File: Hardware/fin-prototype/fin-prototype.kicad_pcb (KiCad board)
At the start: 4 copper layers, 50 x 50 mm, 80 parts, among them J1 USB_C_Receptacle_USB2.0_16P, J10 Conn_01x01_Pin, J11 Conn_01x01_Pin, J12 Conn_01x01_Pin, J13 Conn_01x01_Pin, J14 Conn_01x01_Pin, J15 Conn_01x01_Pin, J16 Conn_01x01_Pin, J17 Conn_01x01_Pin, J18 Conn_01x01_Pin, J2 Conn_01x04_Pin, J3 Conn_01x04_Pin, J4 Conn_01x08_Pin, J5 Conn_01x04_Pin, J6 Conn_01x01_Pin, J7 Conn_01x01_Pin, J8 Conn_01x01_Pin, J9 Conn_01x01_Pin, SW1 SW_Push, SW2 SW_Push, U1 ADS131M03QPWRQ1, U2 STM32L412C8Tx, U3 W25N512GVEIG, U4 TMP235A4DBZR, U5 FT232RNQ-REEL

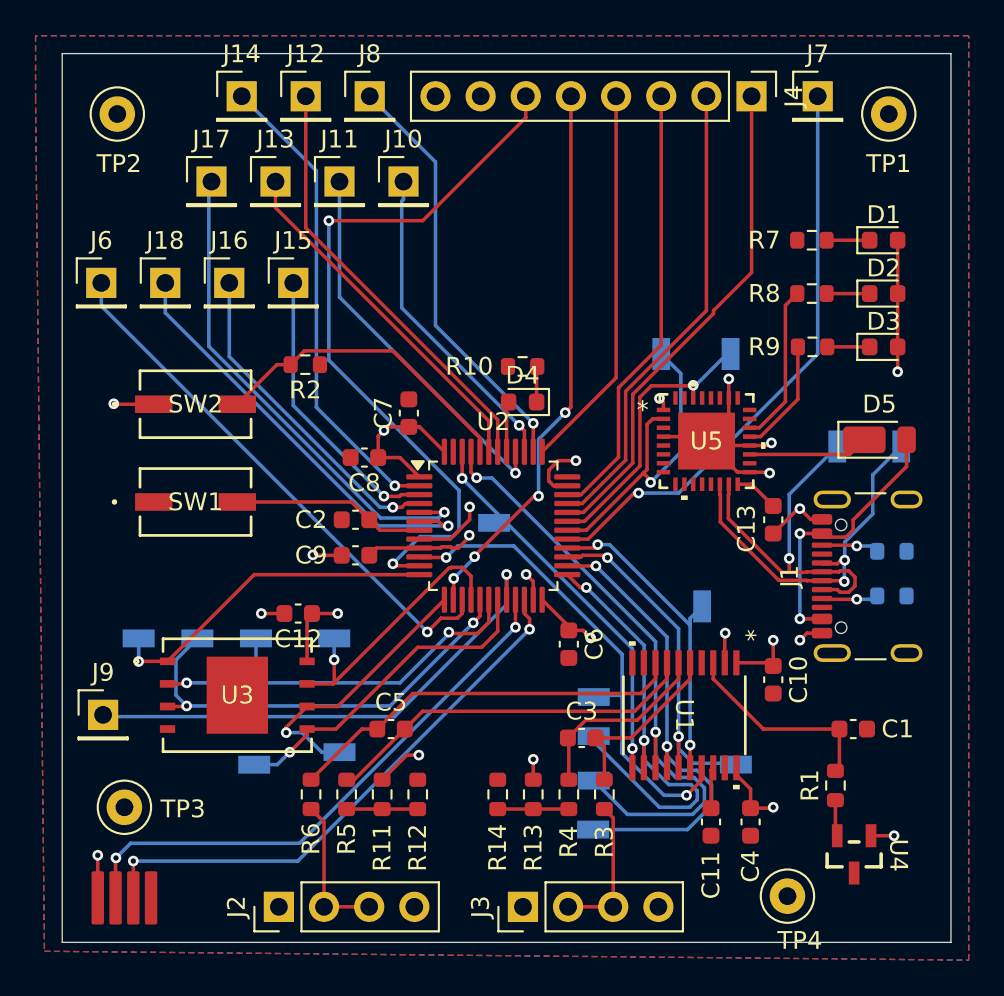
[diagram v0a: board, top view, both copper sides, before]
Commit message: finish up silkscreen
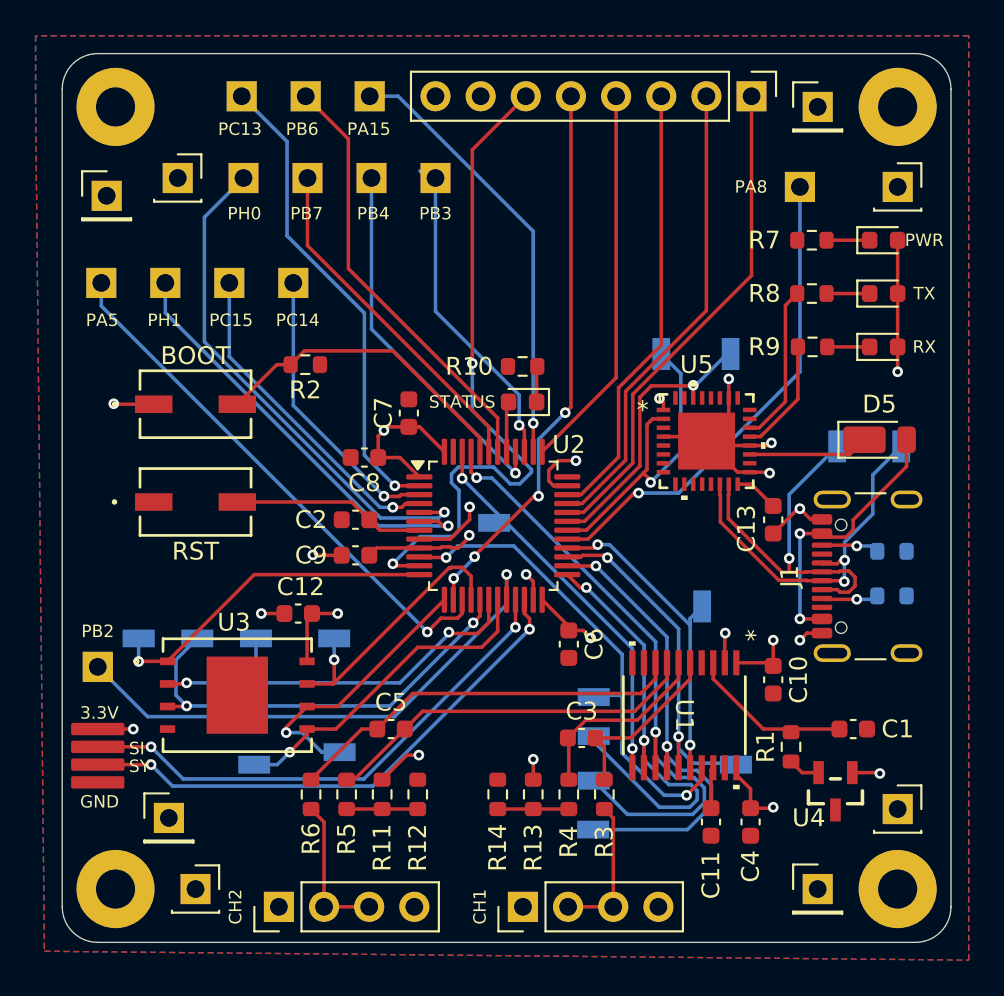
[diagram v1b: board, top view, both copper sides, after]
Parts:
- added H1: MountingHole_Pad, MountingHole:MountingHole_2.2mm_M2_Pad, F.Cu at (97.5, 52.0)
- added H2: MountingHole_Pad, MountingHole:MountingHole_2.2mm_M2_Pad, F.Cu at (141.5, 52.0)
- added H3: MountingHole_Pad, MountingHole:MountingHole_2.2mm_M2_Pad, F.Cu at (141.5, 96.0)
- added H4: MountingHole_Pad, MountingHole:MountingHole_2.2mm_M2_Pad, F.Cu at (97.5, 96.0)
- added TP5: TestPoint, Connector_PinSocket_2.54mm:PinSocket_1x01_P2.54mm_Vertical, F.Cu at (101.0, 56.0)
- added TP6: TestPoint, Connector_PinSocket_2.54mm:PinSocket_1x01_P2.54mm_Vertical, F.Cu at (141.5, 56.5)
- added TP7: TestPoint, Connector_PinSocket_2.54mm:PinSocket_1x01_P2.54mm_Vertical, F.Cu at (141.5, 91.5)
- added TP8: TestPoint, Connector_PinSocket_2.54mm:PinSocket_1x01_P2.54mm_Vertical, F.Cu at (102.0, 96.0)
- J10, J11, J12, J13, J14, J15, J16, J17, J18, J6, J7, J8, J9: footprint Connector_PinHeader_2.54mm:PinHeader_1x01_P2.54mm_Vertical -> FinLib:SimpleThroughHole
- TP1, TP2, TP3, TP4: footprint TestPoint:TestPoint_Loop_D1.80mm_Drill1.0mm_Beaded -> Connector_PinHeader_2.54mm:PinHeader_1x01_P2.54mm_Vertical
- moved J7 5.20 mm to (136.0, 56.5)
- moved TP2 4.64 mm to (97.0, 57.0)
- moved J5 4.62 mm to (101.6, 88.5), turned to -90 degrees
- moved TP1 4.02 mm to (137.0, 52.0)
- moved U4 3.70 mm to (138.0, 90.5)
- moved R1 3.31 mm to (135.5, 88.0)
- moved J9 2.72 mm to (96.5, 83.5)
- moved TP3 2.57 mm to (100.5, 92.0)
- moved J11 1.81 mm to (111.9, 56.0)
- moved J10 1.81 mm to (115.5, 56.0)
- moved J13 1.81 mm to (108.3, 56.0)
- moved J17 1.81 mm to (104.7, 56.0)
- moved TP4 1.75 mm to (137.0, 96.0)
- renumbered TP6 to TP10, TP7 to TP11, TP8 to TP12, TP9 to TP13, TP10 to TP14, TP11 to TP15, TP12 to TP16, TP13 to TP17, TP14 to TP18, TP15 to TP19, TP16 to TP20, TP17 to TP21, TP18 to TP22, TP19 to TP23, TP20 to TP24, TP21 to TP25, TP5 to TP9
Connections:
- net QSPI_CLK renamed QSPI_SCK
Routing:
- net PA8: track 32.9 -> 27.4 mm
- net SPI1_SCK: track 41.2 -> 38.5 mm
- net Net-(U1-AIN0P): track 11.6 -> 9.17 mm
- net SIGNAL: track 31.7 -> 29.3 mm
- net PB2: track 28.5 -> 29.9 mm
- net AVBAY_SYNC: track 31.6 -> 30.2 mm
- net PH0: track 28.1 -> 29.3 mm
- net PA15: track 23.8 -> 24.7 mm
- net PB3: track 18.1 -> 19.0 mm
- net PB4: track 21.7 -> 21.2 mm
- net PB7: track 20.2 -> 19.6 mm
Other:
- outline, holes or cut-outs redrawn
- board text added: "3.3V"
- board text added: "GND"
- board text added: "SI"
- board text added: "SY"
- board text removed: "TODO: Add silkscreen labels TODO: Fix 3.3V layer TODO: See if traces can be routed in a less cursed way"

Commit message: touchup a few things
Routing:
- net GND: vias 11 -> 14
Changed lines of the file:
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@@
 	)
 	(via
+		(at 112.6 67.4)
+		(size 0.6)
+		(drill 0.3)
+		(layers "F.Cu" "B.Cu")
+		(free yes)
+		(net 2)
+	)
+	(via
 		(at 108.6 77.2)
 		(size 0.6)
@@
 	)
 	(via
+		(at 110.2 68)
+		(size 0.6)
+		(drill 0.3)
+		(layers "F.Cu" "B.Cu")
+		(free yes)
+		(net 2)
+	)
+	(via
 		(at 136 74.6)
 		(size 0.6)
@@
 	)
 	(via
+		(at 119.6 61.8)
+		(size 0.6)
+		(drill 0.3)
+		(layers "F.Cu" "B.Cu")
+		(free yes)
+		(net 2)
+	)
+	(via
 		(at 134.4 70.9)
 		(size 0.6)
@@
 	)
 	(segment
-		(start 117.5 78.4)
-		(end 117.5 79.725)
+		(start 109.74 84.46)
+		(end 109.8 84.4)
 		(width 0.2)
 		(layer "F.Cu")
@@
 	)
 	(segment
-		(start 109.74 84.46)
-		(end 109.8 84.4)
+		(start 117.5 78.4)
+		(end 117.5 79.725)
 		(width 0.2)
 		(layer "F.Cu")
@@
 	)
 	(segment
-		(start 109.74 84.46)
-		(end 116.249 77.951)
+		(start 108.275 84.46)
+		(end 109.74 84.46)
 		(width 0.2)
 		(layer "F.Cu")
@@
 	)
 	(segment
-		(start 116.249 77.951)
-		(end 116.348943 77.951)
+		(start 115.923419 78.276581)
+		(end 115.923419 78.275824)
 		(width 0.2)
 		(layer "F.Cu")
@@
 	)
 	(segment
-		(start 117 77.9)
-		(end 117.5 78.4)
+		(start 115.923419 78.275824)
+		(end 116.275476 77.923767)
 		(width 0.2)
 		(layer "F.Cu")
@@
 	)
 	(segment
-		(start 108.275 84.46)
-		(end 109.74 84.46)
+		(start 116.275476 77.923767)
+		(end 117.023767 77.923767)
 		(width 0.2)
 		(layer "F.Cu")
@@
 	)
 	(segment
-		(start 116.399943 77.9)
-		(end 117 77.9)
+		(start 109.74 84.46)
+		(end 115.923419 78.276581)
 		(width 0.2)
 		(layer "F.Cu")
@@
 	)
 	(segment
-		(start 116.348943 77.951)
-		(end 116.399943 77.9)
+		(start 117.023767 77.923767)
+		(end 117.5 78.4)
 		(width 0.2)
 		(layer "F.Cu")

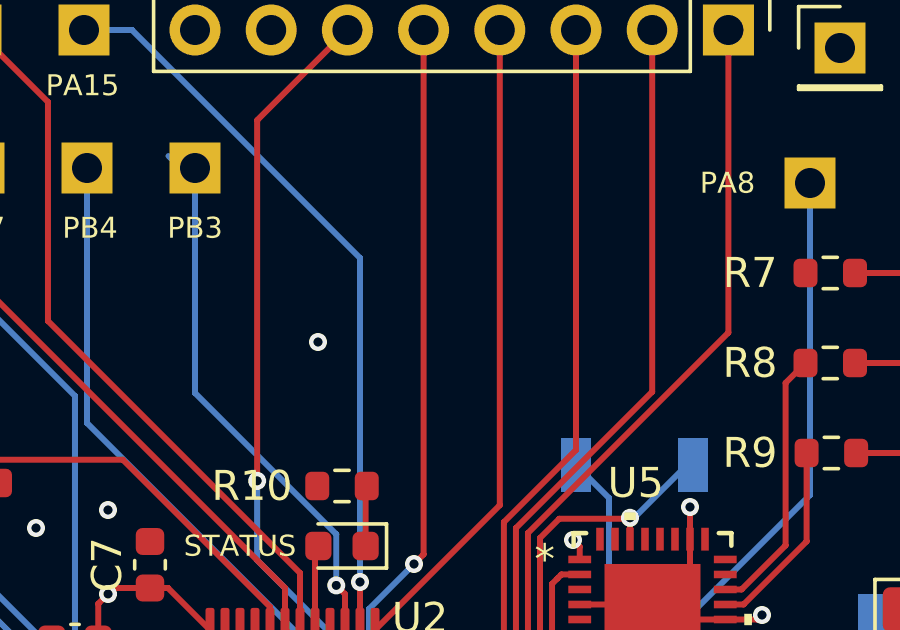
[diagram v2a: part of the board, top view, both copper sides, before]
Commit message: generate fin prototype fab outputs
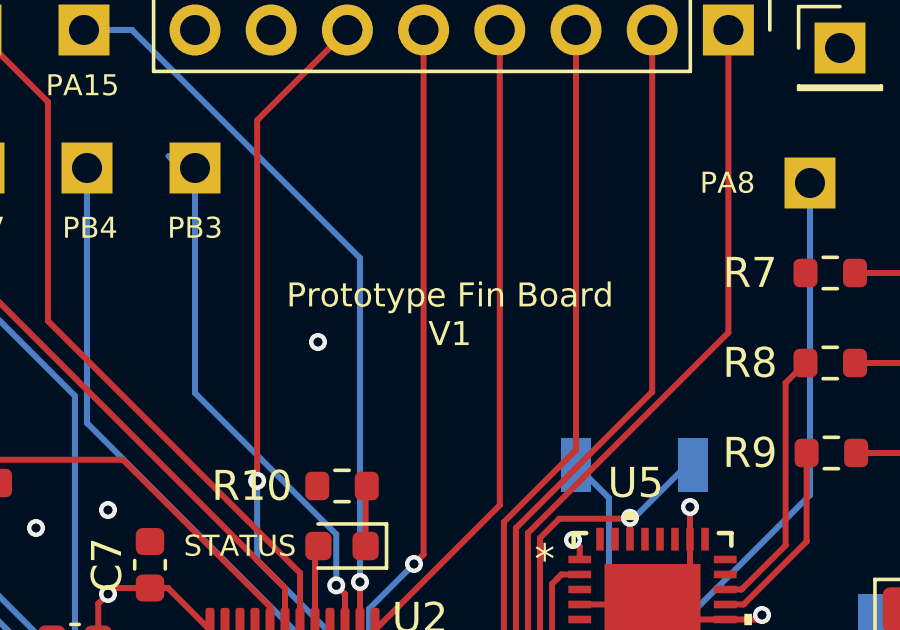
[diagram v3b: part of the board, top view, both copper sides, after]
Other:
- board text added: "Prototype Fin Board V1"
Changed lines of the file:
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@@
+		)
+	)
+	(gr_text "Prototype Fin Board\nV1"
+		(at 124 62 0)
+		(layer "F.SilkS")
+		(effects
+			(font
+				(size 0.8 0.8)
+				(thickness 0.1)
+			)
+			(justify bottom)
 		)
 	)
